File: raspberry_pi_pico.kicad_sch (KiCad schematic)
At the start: 72 parts, among them J10 Conn_01x20_Socket, J2 Conn_02x20_Counter_Clockwise, J3 Conn_02x20_Counter_Clockwise, J4 Conn_01x20_Socket, J7 Conn_01x01_Pin, U3 Pico

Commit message: Getting JLCPCB Price
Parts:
- J10, J2, J3, J4: now fitted
- S1: value Tactile Button, 160gf -> RST
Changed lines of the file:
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@@
 		(on_board yes)
 		(dnp no)
-		(fields_autoplaced yes)
 		(property "Reference" "S1"
 			(at 182.88 146.0499 0)
@@
 			)
 		)
-		(property "Value" "Tactile Button, 160gf"
-			(at 182.88 147.32 0)
+		(property "Value" "RST"
+			(at 183.134 148.59 0)
 			(effects
 				(font
@@
 				)
 				(justify left)
-				(hide yes)
 			)
 		)
@@
 		(in_bom yes)
 		(on_board yes)
-		(dnp yes)
+		(dnp no)
 		(property "Reference" "J4"
 			(at 120.65 90.1699 0)
@@
 		(in_bom yes)
 		(on_board yes)
-		(dnp yes)
+		(dnp no)
 		(fields_autoplaced yes)
 		(property "Reference" "J2"
@@
 		(in_bom yes)
 		(on_board yes)
-		(dnp yes)
+		(dnp no)
 		(fields_autoplaced yes)
 		(property "Reference" "J3"
@@
 		(in_bom yes)
 		(on_board yes)
-		(dnp yes)
+		(dnp no)
 		(property "Reference" "J10"
 			(at 156.21 90.1699 0)

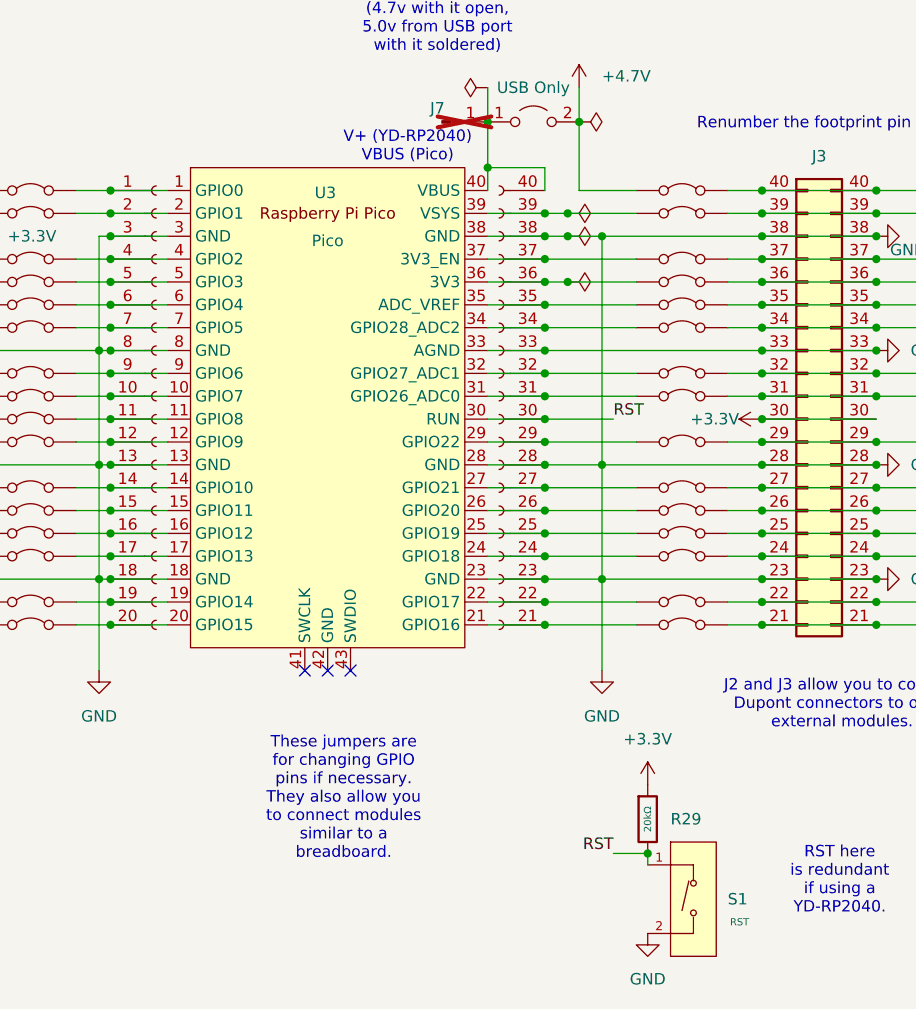
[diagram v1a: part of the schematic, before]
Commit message: Replaced Jaron's LEDs
They were only for Standard Boards.
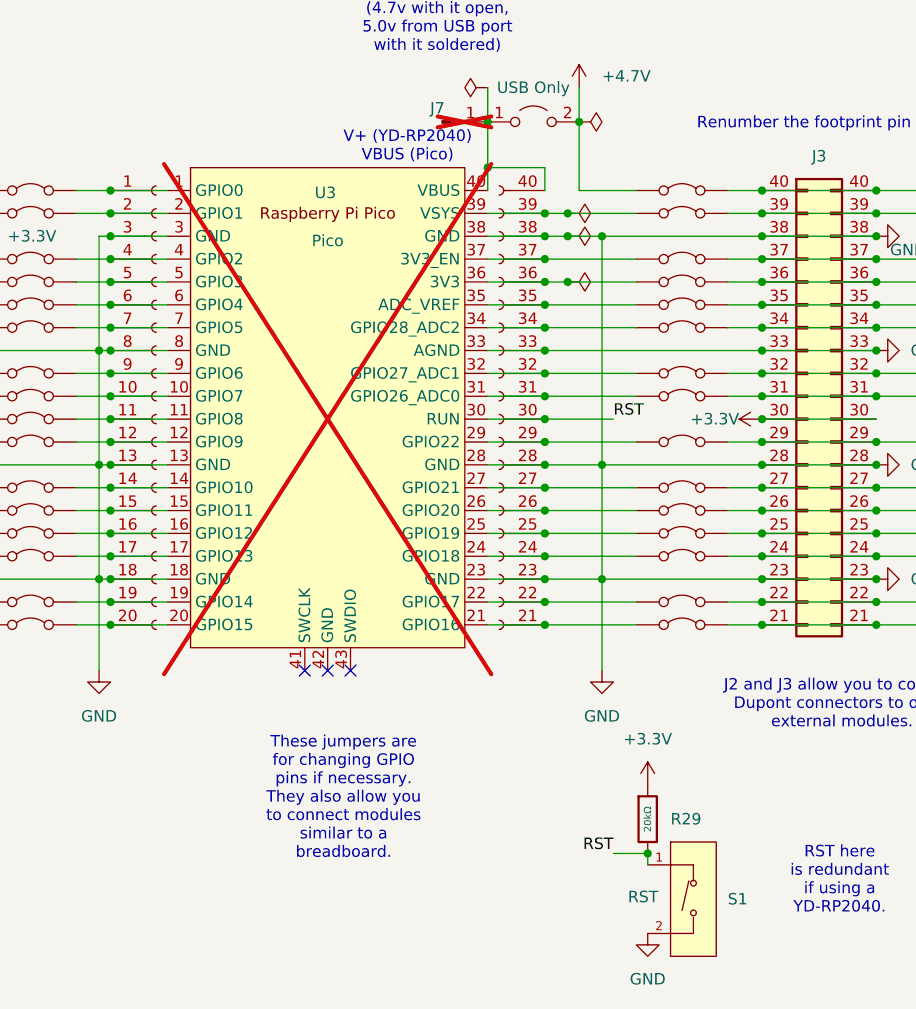
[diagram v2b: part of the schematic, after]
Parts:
- S1: value RST -> Tactile Button, 160gf; Label (none) -> RST
- U3: now not fitted
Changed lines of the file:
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@@
 			)
 		)
-		(property "Value" "RST"
+		(property "Value" "Tactile Button, 160gf"
 			(at 183.134 148.59 0)
 			(effects
@@
 				)
 				(justify left)
+				(hide yes)
 			)
 		)
@@
 				)
 				(hide yes)
+			)
+		)
+		(property "Label" "RST"
+			(at 173.482 145.796 0)
+			(effects
+				(font
+					(size 1.27 1.27)
+				)
 			)
 		)
@@
 		(in_bom yes)
 		(on_board yes)
-		(dnp no)
+		(dnp yes)
 		(property "Reference" "U3"
 			(at 138.176 67.564 0)

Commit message: Initial v0.2
Fixed SCL-SDA swap, 3V3 on encoder, and 3D models for Kicad 10
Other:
- note added: "For the YD-RP2040 we want the USB Only jumper shorted."
- note added: "If you are using a real Pico, this jumper bridges a Schottky diode from USB in to Vsys (4.7v with it open, 5.0v from USB port with it soldered)"
- note removed: "If you are using a real Pico, his jumper bridges a Schottky diode from USB in to Vsys (4.7v with it open, 5.0v from USB port with it soldered)"

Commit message: Starting a new branch for v0.2
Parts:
- removed JP50: USB Only, Jumper:SolderJumper-2_P1.3mm_Open_RoundedPad1.0x1.5mm, symbol Jumper:Jumper_2_Open
- added JP50: USB_ONLY, Jumper:SolderJumper-2_P1.3mm_Bridged2Bar_RoundedPad1.0x1.5mm, symbol Jumper:Jumper_2_Bridged
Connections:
- net +4.7V: now also JP50.1 (A)
- net at J10.40 (Pin_1), J7.1 (Pin_1), U3.40 (VBUS): now also JP50.2 (B)
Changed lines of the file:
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@@
 	(generator_version "10.0")
 	(paper "USLetter")
+	(title_block
+		(date "2026-03-31")
+		(rev "0.2")
+	)
 	(text "J2 and J3 allow you to connect \nDupont connectors to other \nexternal modules."
 		(exclude_from_sim no)
@@
 	)
 	(symbol
-		(lib_id "Jumper:Jumper_2_Open")
-		(at 161.29 59.69 0)
-		(unit 1)
-		(body_style 1)
-		(exclude_from_sim no)
-		(in_bom yes)
-		(on_board yes)
-		(in_pos_files yes)
-		(dnp no)
-		(fields_autoplaced yes)
-		(property "Reference" "JP50"
-			(at 161.29 53.34 0)
-			(hide yes)
-			(show_name no)
-			(do_not_autoplace no)
-			(effects
-				(font
-					(size 1.27 1.27)
-				)
-			)
-		)
-		(property "Value" "USB Only"
-			(at 161.29 55.88 0)
-			(show_name no)
-			(do_not_autoplace no)
-			(effects
-				(font
-					(size 1.27 1.27)
-				)
-			)
-		)
-		(property "Footprint" "Jumper:SolderJumper-2_P1.3mm_Open_RoundedPad1.0x1.5mm"
-			(at 161.29 59.69 0)
-			(hide yes)
-			(show_name no)
-			(do_not_autoplace no)
-			(effects
-				(font
-					(size 1.27 1.27)
-				)
-			)
-		)
-		(property "Datasheet" ""
-			(at 161.29 59.69 0)
-			(hide yes)
-			(show_name no)
-			(do_not_autoplace no)
-			(effects
-				(font
-					(size 1.27 1.27)
-				)
-			)
-		)
-		(property "Description" ""
-			(at 161.29 59.69 0)
-			(hide yes)
-			(show_name no)
-			(do_not_autoplace no)
-			(effects
-				(font
-					(size 1.27 1.27)
-				)
-			)
-		)
-		(property "JLCPCB #" ""
-			(at 161.29 59.69 0)
-			(hide yes)
-			(show_name no)
-			(do_not_autoplace no)
-			(effects
-				(font
-					(size 1.27 1.27)
-				)
-			)
-		)
-		(pin "1"
-		)
-		(pin "2"
-		)
-		(instances
-			(project "PCM1808_Sound_Card"
-				(path "/04b4b624-9c46-4205-aa19-e3356b229b17/06516c79-bfe4-40ed-9cd2-382c74eaa2ba"
-					(reference "JP50")
-					(unit 1)
-				)
-			)
-			(project "Intro-to-CAD-2026"
-				(path "/c12dc015-e6cb-468c-8de4-269c3106de0e/ed44bed7-549c-4a19-9507-4d924c35e7b0"
-					(reference "JP50")
-					(unit 1)
-				)
-			)
-		)
-	)
-	(symbol
 		(lib_id "power:+3.3V")
 		(at 99.06 72.39 270)
@@
 					(unit 1)
 				)
+			)
+		)
+	)
+	(symbol
+		(lib_id "Jumper:Jumper_2_Bridged")
+		(at 161.29 59.69 0)
+		(mirror y)
+		(unit 1)
+		(body_style 1)
+		(exclude_from_sim yes)
+		(in_bom yes)
+		(on_board yes)
+		(in_pos_files yes)
+		(dnp no)
+		(fields_autoplaced yes)
+		(property "Reference" "JP50"
+			(at 161.29 57.15 0)
+			(hide yes)
+			(show_name no)
+			(do_not_autoplace no)
+			(effects
+				(font
+					(size 1.27 1.27)
+				)
+			)
+		)
+		(property "Value" "USB_ONLY"
+			(at 161.29 57.15 0)
+			(show_name no)
+			(do_not_autoplace no)
+			(effects
+				(font
+					(size 1.27 1.27)
+				)
+			)
+		)
+		(property "Footprint" "Jumper:SolderJumper-2_P1.3mm_Bridged2Bar_RoundedPad1.0x1.5mm"
+			(at 161.29 59.69 0)
+			(hide yes)
+			(show_name no)
+			(do_not_autoplace no)
+			(effects
+				(font
+					(size 1.27 1.27)
+				)
+			)
+		)
+		(property "Datasheet" ""
+			(at 161.29 59.69 0)
+			(hide yes)
+			(show_name no)
+			(do_not_autoplace no)
+			(effects
+				(font
+					(size 1.27 1.27)
+				)
+			)
+		)
+		(property "Description" "Jumper, 2-pole, closed/bridged"
+			(at 161.29 59.69 0)
+			(hide yes)
+			(show_name no)
+			(do_not_autoplace no)
+			(effects
+				(font
+					(size 1.27 1.27)
+				)
+			)
+		)
+		(property "JLCPCB #" ""
+			(at 161.29 59.69 0)
+			(hide yes)
+			(show_name no)
+			(do_not_autoplace no)
+			(effects
+				(font
+					(size 1.27 1.27)
+				)
+			)
+		)
+		(pin "2"
+		)
+		(pin "1"
+		)
+		(instances
+			(project "Intro-to-CAD-2026"
+				(path "/c12dc015-e6cb-468c-8de4-269c3106de0e/ed44bed7-549c-4a19-9507-4d924c35e7b0"
+					(reference "JP50")
+					(unit 1)
+				)

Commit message: Placed the second ADC
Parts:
- C39: Manufacturer AVX -> (none)
- R29: Manufacturer UNI-ROYAL(Uniroyal Elec) -> (none)
- S1: Manufacturer XUNPU -> (none)
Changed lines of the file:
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@@
 			)
 		)
-		(property "Manufacturer" "XUNPU"
-			(at 179.07 144.78 0)
-			(hide yes)
-			(show_name no)
-			(do_not_autoplace no)
-			(effects
-				(font
-					(size 1.27 1.27)
-				)
-			)
-		)
 		(property "Part" "TS-1088-AR02016"
 			(at 179.07 144.78 0)
@@
 			)
 		)
-		(property "Manufacturer" "AVX"
-			(at 234.95 81.28 0)
-			(hide yes)
-			(show_name no)
-			(do_not_autoplace no)
-			(effects
-				(font
-					(size 1.27 1.27)
-				)
-			)
-		)
 		(property "Part" "TAJA106K016RNJ"
 			(at 234.95 81.28 0)
@@
 			(at 173.99 137.16 0)
 			(hide yes)
-			(show_name no)
-			(do_not_autoplace no)
-			(effects
-				(font
-					(size 1.27 1.27)
-				)
-			)
-		)
-		(property "Manufacturer" "UNI-ROYAL(Uniroyal Elec)"
-			(at 173.99 137.16 0)
-			(hide yes)
